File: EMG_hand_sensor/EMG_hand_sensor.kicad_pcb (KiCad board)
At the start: 2 copper layers, 39 parts, among them J1 Conn_2Rows-07Pins_Shielded, J2 B2B-XH-A, U1 TVS0500DRV, U10 TRS_AUDIO_JACK_3.5mm, U11 TRS_AUDIO_JACK_3.5mm, U2 ADA4099-2xR, U3 CD74HC4067M, U4 TRS_AUDIO_JACK_3.5mm, U6 ADA4099-2xR, U7 LT1762, U8 TRS_AUDIO_JACK_3.5mm

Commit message: new schematic done
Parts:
- removed R11, R16: 15k, Resistor_SMD:R_0805_2012Metric_Pad1.20x1.40mm_HandSolder
- removed R12, R14, R15, R17, R18: 10k, Resistor_SMD:R_0805_2012Metric_Pad1.20x1.40mm_HandSolder
- removed R13: 100R, Resistor_SMD:R_0805_2012Metric_Pad1.20x1.40mm_HandSolder
- added C12: 1uF, Capacitor_SMD:C_0805_2012Metric_Pad1.18x1.45mm_HandSolder, F.Cu at (172.6, 95.6)
- added C13: 100n, Capacitor_SMD:C_0805_2012Metric_Pad1.18x1.45mm_HandSolder, F.Cu at (172.6, 98.6)
- added C14: 10p, Capacitor_SMD:C_0805_2012Metric_Pad1.18x1.45mm_HandSolder, F.Cu at (172.6, 101.6)
- added C15: 10p, Capacitor_SMD:C_0805_2012Metric_Pad1.18x1.45mm_HandSolder, F.Cu at (172.6, 104.6)
- added C7: 10nF, Capacitor_SMD:C_0805_2012Metric_Pad1.18x1.45mm_HandSolder, F.Cu at (167.8, 98.6)
- added D1: RED, Diode_SMD:D_0805_2012Metric, F.Cu at (141.7, 113.7)
- added FB1: 120R, Resistor_SMD:R_0805_2012Metric_Pad1.20x1.40mm_HandSolder, F.Cu at (141.8, 88.1)
- added SW1: SW_SPDT, Relay_THT:Relay_SPDT_Omron_G6E, F.Cu at (151.0, 89.2)
- added U5: INA128, INA:SOIC127P600X175-8N, F.Cu at (135.2, 96.5)
- added U9: INA128, INA:SOIC127P600X175-8N, F.Cu at (135.2, 109.5)
- added Y1: 16MHz, Crystal:Crystal_SMD_3225-4Pin_3.2x2.5mm, F.Cu at (170.6, 111.4)
- C1: value 100nF -> 10uF
- C2: value 10uF -> 100nF
- C3: value 33nF -> 100nF
- C4, C5: value 470nF -> 100nF
- C6: value 1uF -> 100nF
- C8: value 33nF -> 1uF
- J1: value Conn_2Rows-07Pins_Shielded -> USB_C_Receptacle_USB2.0_16P; footprint Connector_PinHeader_2.54mm:PinHeader_1x07_P2.54mm_Vertical_SMD_Pin1Left -> Connector_Molex:Molex_CLIK-Mate_502386-0970_1x09-1MP_P1.25mm_Horizontal
- J2: value B2B-XH-A -> Conn_01x04_Pin; footprint Connector_JST:JST_EH_B2B-EH-A_1x02_P2.50mm_Vertical -> Connector_PinHeader_2.54mm:PinHeader_1x04_P2.54mm_Vertical
- R10, R5: value 10k -> 500
- R2: value 1k -> 1k5
- R6: value 1k -> 500
- R7: value 18k -> 500
- R8, R9: value 10k -> 5k1
- U1: value TVS0500DRV -> USBLC6-2SC6; footprint Package_SON:WSON-6-1EP_2x2mm_P0.65mm_EP1x1.6mm -> Package_TO_SOT_SMD:SOT-23-6
- U2: value ADA4099-2xR -> STM32F103C8Tx; footprint Package_SO:SOIC-8_3.9x4.9mm_P1.27mm -> Package_QFP:LQFP-48_7x7mm_P0.5mm
- U3: value CD74HC4067M -> INA128; footprint Package_SO:SOIC-24W_7.5x15.4mm_P1.27mm -> INA:SOIC127P600X175-8N
- U6: value ADA4099-2xR -> INA128; footprint Package_SO:SOIC-8_3.9x4.9mm_P1.27mm -> INA:SOIC127P600X175-8N
- moved C11 83.4 mm to (167.8, 107.6)
- moved C8 83.4 mm to (167.8, 101.6)
- moved C9 83.4 mm to (167.8, 104.6)
- moved C6 83.1 mm to (167.8, 95.6)
- moved C1 80.9 mm to (163.0, 95.6)
- moved C2 80.9 mm to (163.0, 98.6)
- moved C3 80.9 mm to (163.0, 101.6)
- moved C4 80.9 mm to (163.0, 104.6)
- moved C5 80.9 mm to (163.0, 107.6)
- moved J2 64.5 mm to (177.3, 96.4)
- moved J1 63.9 mm to (168.9, 90.3)
- moved U7 61.2 mm to (164.3, 111.5)
- moved R6 57.0 mm to (146.6, 88.1)
- moved R7 57.0 mm to (146.6, 91.0)
- moved R10 55.7 mm to (146.6, 99.9)
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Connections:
- C1 pad 1: +3V3 -> +3.3V
- C10 pad 1: /+3v3 -> +3.3V
- C11 pad 1: /+3v3 -> +3.3V
- C2 pad 1: +3V3 -> +3.3V
- C3 pad 1: Net-(C3-Pad1) -> +3.3V
- C3 pad 2: EMG_analog_signal -> GND
- C4 pad 1: Net-(C4-Pad1) -> +3.3V
- C4 pad 2: Net-(U2B-+) -> GND
- C5 pad 1: EMG_analog_signal -> +3.3V
- C5 pad 2: Net-(C4-Pad1) -> GND
- C6 pad 1: EMG_analog_signal -> +3.3V
- C8 pad 1: Net-(U6A-+) -> +3.3VA
- C9 pad 1: /VBAT -> VBUS
- J1 pad 1: ¬Enable -> (no net)
- J1 pad 2: EMG_analog_signal -> (no net)
- J1 pad 3: S0 -> (no net)
- J1 pad 4: S2 -> (no net)
- J1 pad 5: S1 -> (no net)
- J1 pad 6: GND -> (no net)
- J1 pad 7: S3 -> (no net)
- J2 pad 1: GND -> +3.3V
- J2 pad 2: /VBAT -> /SWDIO
- R1 pad 1: EMG_analog_signal -> /SW_BOOT0
- R1 pad 2: Net-(C3-Pad1) -> /BOOT0
- R10 pad 2: Net-(U2B--) -> Net-(R10-Pad2)
- R2 pad 1: EMG_analog_signal -> Net-(D1-K)
- R2 pad 2: Net-(U6A--) -> GND
- R3 pad 1: Net-(U6A--) -> +3.3V
- R3 pad 2: GND -> /+1v6
- R4 pad 1: S3 -> /+1v6
- R5 pad 1: S2 -> Net-(R5-Pad1)
- R5 pad 2: GND -> Net-(R5-Pad2)
- R6 pad 1: EMG_analog_signal -> Net-(R6-Pad1)
- R6 pad 2: Net-(R10-Pad1) -> Net-(R6-Pad2)
- R7 pad 1: Net-(U2B--) -> Net-(R7-Pad1)
- R7 pad 2: GND -> Net-(R7-Pad2)
- R8 pad 1: GND -> Net-(J1-CC1)
- R8 pad 2: S0 -> GND
- R9 pad 1: Net-(U6A-+) -> /CC2
- R9 pad 2: Net-(C3-Pad1) -> GND
- U1 pad 1: GND -> Net-(J1-D--PadA7)
- U1 pad 3: GND -> Net-(J1-D+-PadA6)
- U1 pad 4: EMG_analog_signal -> /USB_D+
- U1 pad 5: EMG_analog_signal -> VBUS
- U1 pad 6: EMG_analog_signal -> /USB_D-
- U2 pad 1: EMG_analog_signal -> +3.3V
- U2 pad 2: EMG_analog_signal -> unconnected-(U2-PC13-Pad2)
- U2 pad 3: EMG_analog_signal -> unconnected-(U2-PC14-Pad3)
- U2 pad 4: (no net) -> unconnected-(U2-PC15-Pad4)
- U2 pad 5: Net-(U2B-+) -> /HSE_IN
- U2 pad 6: Net-(U2B--) -> /HSE_LOW
- U2 pad 7: Net-(R10-Pad1) -> /NRST
- U2 pad 8: (no net) -> GND
- U3 pad 1: EMG_analog_signal -> Net-(R5-Pad1)
- U3 pad 2: E8 -> E2
- U3 pad 3: E7 -> E1
- U3 pad 4: E6 -> GND
- U3 pad 5: E5 -> /+1v6
- U3 pad 6: E4 -> E1
- U3 pad 7: E3 -> +3.3V
- U3 pad 8: E2 -> Net-(R5-Pad2)
- U6 pad 1: EMG_analog_signal -> Net-(R7-Pad1)
- U6 pad 2: Net-(U6A--) -> E4
- U6 pad 3: Net-(U6A-+) -> E3
- U6 pad 4: (no net) -> GND
- U6 pad 5: EMG_analog_signal -> /+1v6
- U6 pad 6: Net-(U6B--) -> E3
- U6 pad 7: EMG_analog_signal -> +3.3V
- U6 pad 8: (no net) -> Net-(R7-Pad2)
- U7 pad 1: /+3v3 -> +3.3V
- U7 pad 2: /+3v3 -> +3.3V
- U7 pad 5: /VBAT -> VBUS
- U7 pad 8: /VBAT -> VBUS

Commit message: pcb design started layout
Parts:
- moved U6 62.8 mm to (196.3, 88.4)
- moved U5 61.2 mm to (193.0, 76.5)
- moved U4 58.7 mm to (194.6, 65.3), turned to 90 degrees
- moved U9 52.0 mm to (186.3, 99.9)
- moved SW1 48.7 mm to (134.0, 43.5)
- moved U10 45.9 mm to (194.0, 109.5), turned to -90 degrees
- moved U3 45.1 mm to (178.3, 76.6)
- moved D1 43.6 mm to (168.1, 79.0)
- moved J2 37.1 mm to (148.9, 72.5), turned to 90 degrees
- moved U11 35.8 mm to (208.3, 86.6)
- moved U2 31.2 mm to (176.7, 87.8)
- moved U1 28.2 mm to (162.9, 86.5)
- moved U8 26.6 mm to (172.9, 64.8), turned to -90 degrees
- moved J1 26.1 mm to (143.2, 86.0), turned to -90 degrees
- moved R1 20.7 mm to (124.2, 80.1)
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
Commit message: starting pch layout
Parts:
- removed U10, U11, U4, U8: TRS_AUDIO_JACK_3.5mm, Connector_Audio:Jack_3.5mm_CUI_SJ-3523-SMT_Horizontal
- added J3: AudioJack3, Connector_Audio:Jack_3.5mm_CUI_SJ-3523-SMT_Horizontal, F.Cu at (203.0, 102.0)
- added J4: AudioJack3, Connector_Audio:Jack_3.5mm_CUI_SJ-3523-SMT_Horizontal, F.Cu at (183.0, 64.0)
- added J5: AudioJack3, Connector_Audio:Jack_3.5mm_CUI_SJ-3523-SMT_Horizontal, F.Cu at (162.4, 66.3)
- added J6: AudioJack3, Connector_Audio:Jack_3.5mm_CUI_SJ-3523-SMT_Horizontal, F.Cu at (203.0, 78.5)
- J1: footprint Connector_Molex:Molex_CLIK-Mate_502386-0970_1x09-1MP_P1.25mm_Horizontal -> Connector_USB:USB_C_Receptacle_GCT_USB4105-xx-A_16P_TopMnt_Horizontal
- SW1: footprint Relay_THT:Relay_SPDT_Omron_G6E -> Button_Switch_SMD:SW_SPDT_CK_JS102011SAQN
- moved C15 91.9 mm to (74.3, 99.5)
- moved SW1 71.6 mm to (177.0, 100.8)
- moved D1 49.9 mm to (120.4, 64.0)
- moved J2 30.5 mm to (169.5, 95.0), turned to 0 degrees
- moved C11 24.7 mm to (142.5, 132.0)
- moved C13 24.7 mm to (147.3, 123.0)
- moved C14 24.7 mm to (147.3, 126.0)
- moved C2 24.7 mm to (137.7, 123.0)
- moved C3 24.7 mm to (137.7, 126.0)
- moved C4 24.7 mm to (137.7, 129.0)
- moved C5 24.7 mm to (137.7, 132.0)
- moved C7 24.7 mm to (142.5, 123.0)
- moved C8 24.7 mm to (142.5, 126.0)
- moved C9 24.7 mm to (142.5, 129.0)
- moved C1 24.7 mm to (137.7, 120.0)
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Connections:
- U2 pad 10: E1 -> /O1
- U2 pad 11: E4 -> /O2
- U2 pad 12: E3 -> /O3
- U2 pad 13: E1 -> /O4
- U3 pad 2: E2 -> /E2
- U3 pad 3: E1 -> /E1
- U3 pad 6: E1 -> /O4
- U5 pad 2: E6 -> /E8
- U5 pad 3: E5 -> /E7
- U5 pad 6: E4 -> /O3
- U6 pad 2: E4 -> /E4
- U6 pad 3: E3 -> /E3
- U6 pad 6: E3 -> /O1
- U9 pad 2: E6 -> /E6
- U9 pad 3: E5 -> /E5
- U9 pad 6: E4 -> /O2

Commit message: design rules
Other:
- copper layers 2 -> 4
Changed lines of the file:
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@@
 	(generator_version "9.0")
 	(general
-		(thickness 1.6)
+		(thickness 1.6062)
 		(legacy_teardrops no)
 	)
@@
 	(layers
 		(0 "F.Cu" signal)
+		(4 "In1.Cu" signal)
+		(6 "In2.Cu" signal)
 		(2 "B.Cu" signal)
 		(9 "F.Adhes" user "F.Adhesive")
@@
 	)
 	(setup
+		(stackup
+			(layer "F.SilkS"
+				(type "Top Silk Screen")
+			)
+			(layer "F.Paste"
+				(type "Top Solder Paste")
+			)
+			(layer "F.Mask"
+				(type "Top Solder Mask")
+				(thickness 0.01)
+			)
+			(layer "F.Cu"
+				(type "copper")
+				(thickness 0.035)
+			)
+			(layer "dielectric 1"
+				(type "prepreg")
+				(thickness 0.2104)
+				(material "FR-4")
+				(epsilon_r 4.4)
+				(loss_tangent 0.02)
+			)
+			(layer "In1.Cu"
+				(type "copper")
+				(thickness 0.0152)
+			)
+			(layer "dielectric 2"
+				(type "core")
+				(thickness 1.065)
+				(material "FR-4")
+				(epsilon_r 4.6)
+				(loss_tangent 0.02)
+			)
+			(layer "In2.Cu"
+				(type "copper")
+				(thickness 0.0152)
+			)
+			(layer "dielectric 3"
+				(type "prepreg")
+				(thickness 0.2104)
+				(material "FR-4")
+				(epsilon_r 4.4)
+				(loss_tangent 0.02)
+			)
+			(layer "B.Cu"
+				(type "copper")
+				(thickness 0.035)
+			)
+			(layer "B.Mask"
+				(type "Bottom Solder Mask")
+				(thickness 0.01)
+			)
+			(layer "B.Paste"
+				(type "Bottom Solder Paste")
+			)
+			(layer "B.SilkS"
+				(type "Bottom Silk Screen")
+			)
+			(copper_finish "None")
+			(dielectric_constraints yes)
+		)
 		(pad_to_mask_clearance 0)
 		(allow_soldermask_bridges_in_footprints no)

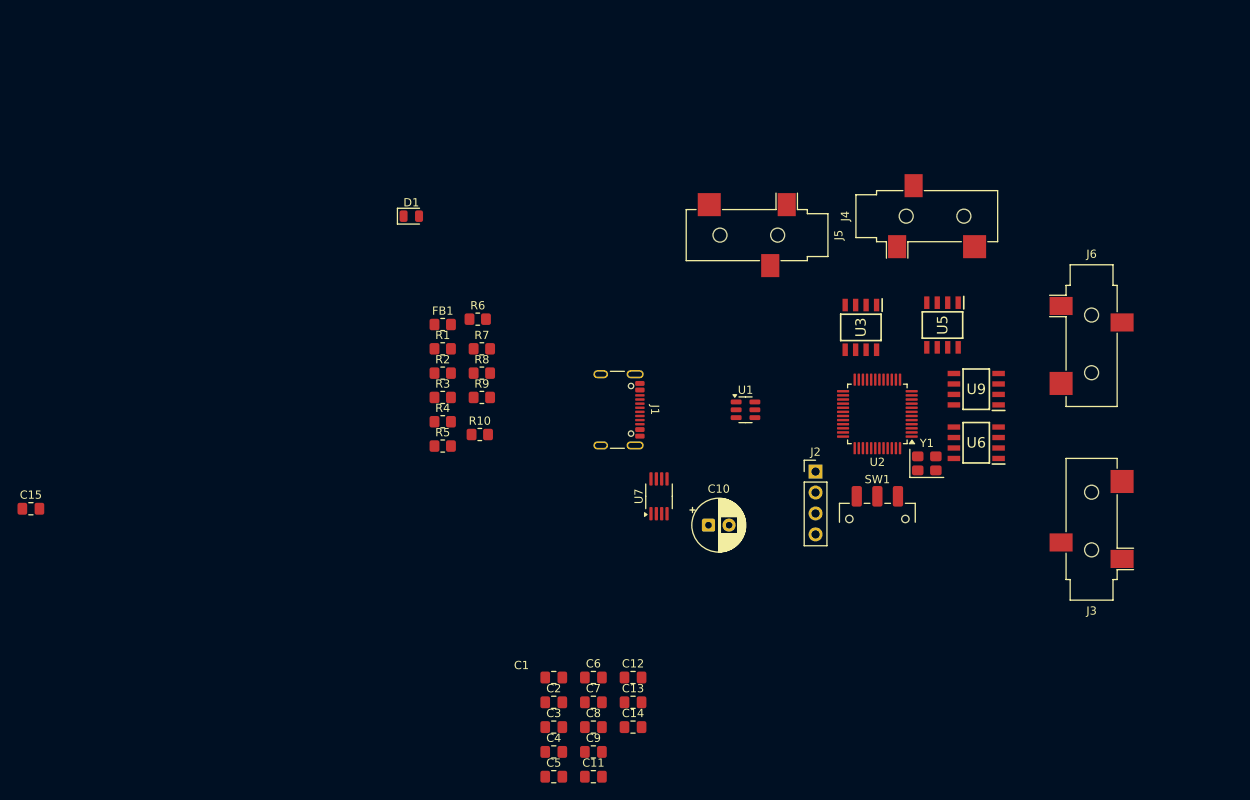
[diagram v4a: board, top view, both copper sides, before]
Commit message: pcb layout finished
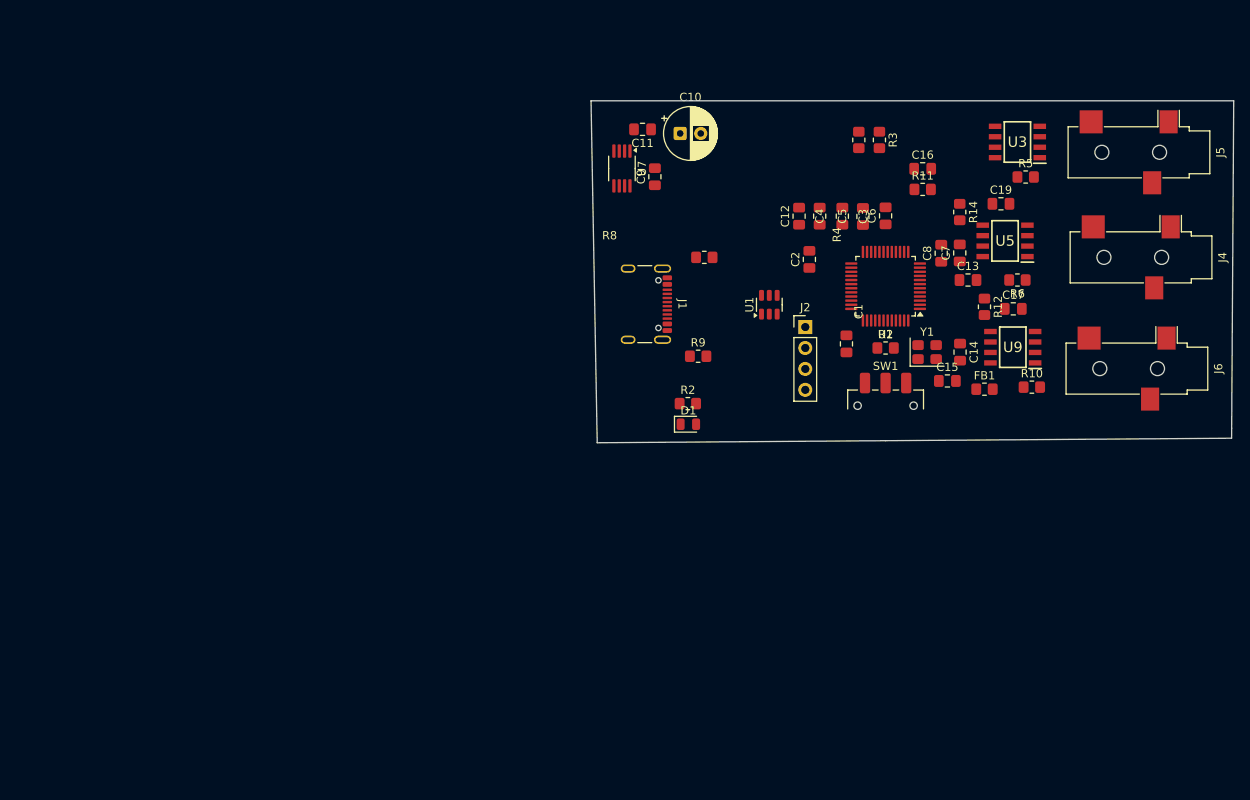
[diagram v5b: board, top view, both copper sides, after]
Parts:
- removed J3: AudioJack3, Connector_Audio:Jack_3.5mm_CUI_SJ-3523-SMT_Horizontal
- removed R7: 500, Resistor_SMD:R_0805_2012Metric_Pad1.20x1.40mm_HandSolder
- removed U6: INA128, INA:SOIC127P600X175-8N
- added C16: 100nF, Capacitor_SMD:C_0805_2012Metric_Pad1.18x1.45mm_HandSolder, F.Cu at (182.5, 58.2)
- added C17: 100nF, Capacitor_SMD:C_0805_2012Metric_Pad1.18x1.45mm_HandSolder, F.Cu at (193.5, 75.2)
- added C19: 100nF, Capacitor_SMD:C_0805_2012Metric_Pad1.18x1.45mm_HandSolder, F.Cu at (192.0, 62.5)
- added R11: 3.3k, Resistor_SMD:R_0805_2012Metric_Pad1.20x1.40mm_HandSolder, F.Cu at (182.5, 60.8)
- added R12: 3.3k, Resistor_SMD:R_0805_2012Metric_Pad1.20x1.40mm_HandSolder, F.Cu at (190.0, 75.0)
- added R14: 3.3k, Resistor_SMD:R_0805_2012Metric_Pad1.20x1.40mm_HandSolder, F.Cu at (187.0, 63.5)
- R10, R5, R6: value 500 -> 50R
- moved C15 112.3 mm to (185.5, 84.0)
- moved C11 78.8 mm to (148.5, 53.5), turned to 180 degrees
- moved R5 77.9 mm to (195.0, 59.2)
- moved C5 76.5 mm to (172.8, 64.0), turned to 90 degrees
- moved C4 72.6 mm to (170.0, 64.0), turned to 90 degrees
- moved C3 72.4 mm to (175.2, 64.0), turned to 90 degrees
- moved C8 71.3 mm to (184.8, 68.5), turned to 90 degrees
- moved C7 70.4 mm to (187.0, 68.5), turned to 90 degrees
- moved C9 70.2 mm to (150.0, 59.2), turned to 90 degrees
- moved R10 67.2 mm to (195.8, 84.8)
- moved C6 66.3 mm to (178.0, 64.0), turned to 90 degrees
- moved FB1 66.2 mm to (190.0, 85.0)
- moved R6 65.7 mm to (194.0, 71.8), turned to 180 degrees
- moved C13 65.4 mm to (188.0, 71.8)
- moved C2 62.1 mm to (168.8, 69.2), turned to 90 degrees
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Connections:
- net /+1v6 renamed +1V6
- net /SWCLK renamed /SWD_CLK
- net /SWDIO renamed /SWD_IO
- J1 pad A6: Net-(J1-D+-PadA6) -> /USB_D+
- J1 pad A7: Net-(J1-D--PadA7) -> /USB_D-
- J1 pad B6: Net-(J1-D+-PadA6) -> /USB_D+
- J1 pad B7: Net-(J1-D--PadA7) -> /USB_D-
- U1 pad 1: Net-(J1-D--PadA7) -> /USB_D-
- U1 pad 3: Net-(J1-D+-PadA6) -> /USB_D+
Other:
- board outline added: 78 x 41.5 mm

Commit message: routing time
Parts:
- moved R5 6.40 mm to (191.0, 54.2), turned to -90 degrees
- moved R10 5.70 mm to (191.2, 81.2), turned to -90 degrees
- moved C10 5.26 mm to (156.6, 57.9)
- moved C11 5.26 mm to (152.0, 57.4)
- moved C9 5.26 mm to (153.5, 63.1)
- moved U7 5.26 mm to (149.5, 62.1)
- moved R3 4.25 mm to (173.5, 56.8)
- moved R4 4.25 mm to (171.0, 56.8)
- moved FB1 3.95 mm to (187.8, 88.2)
- moved U9 2.61 mm to (195.5, 81.5), turned to -90 degrees
- moved U3 1.77 mm to (195.8, 54.8), turned to -90 degrees
- moved C19 1.00 mm to (191.0, 62.5)
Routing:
- net /E6: track 0.00 -> 1.49 mm
- added copper zone on In1.Cu, net GND
- added copper zone on In2.Cu, net GND

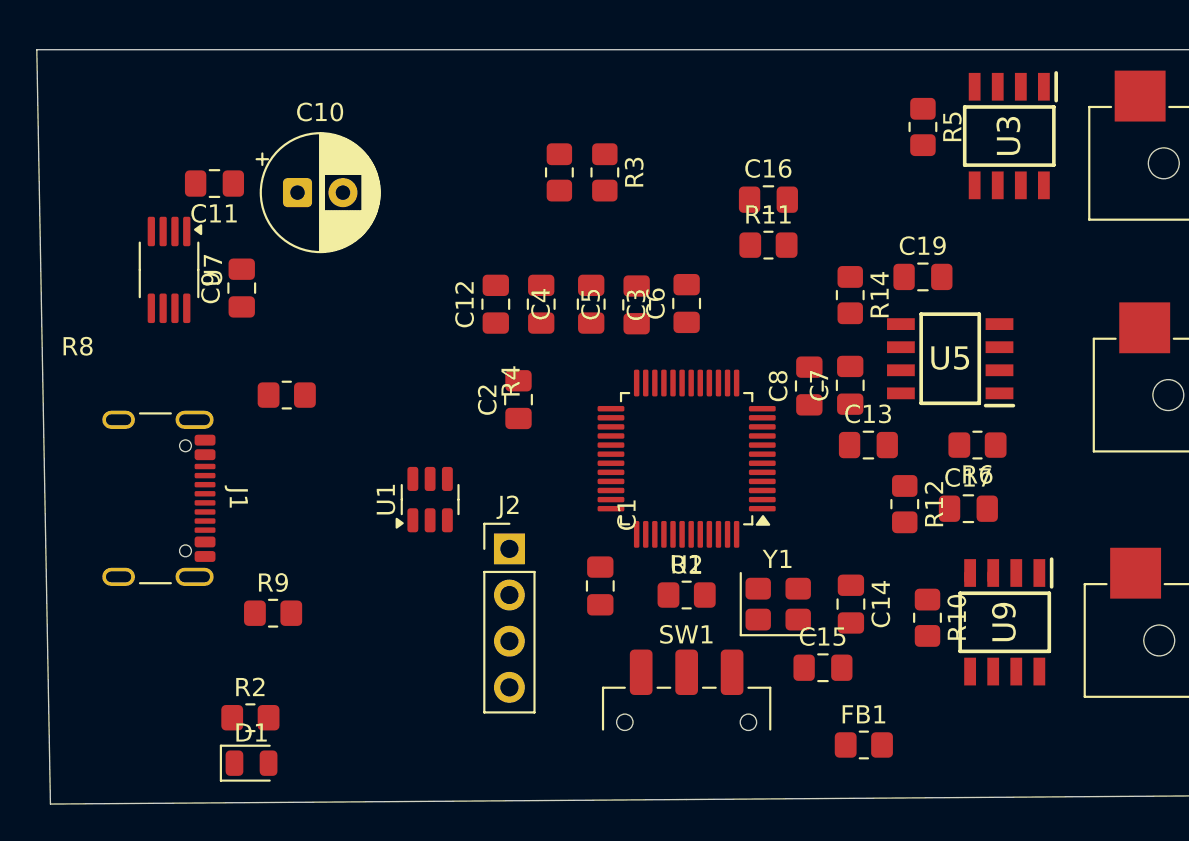
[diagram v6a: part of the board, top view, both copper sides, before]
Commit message: Need to add guard traces and vias and then I can start routing
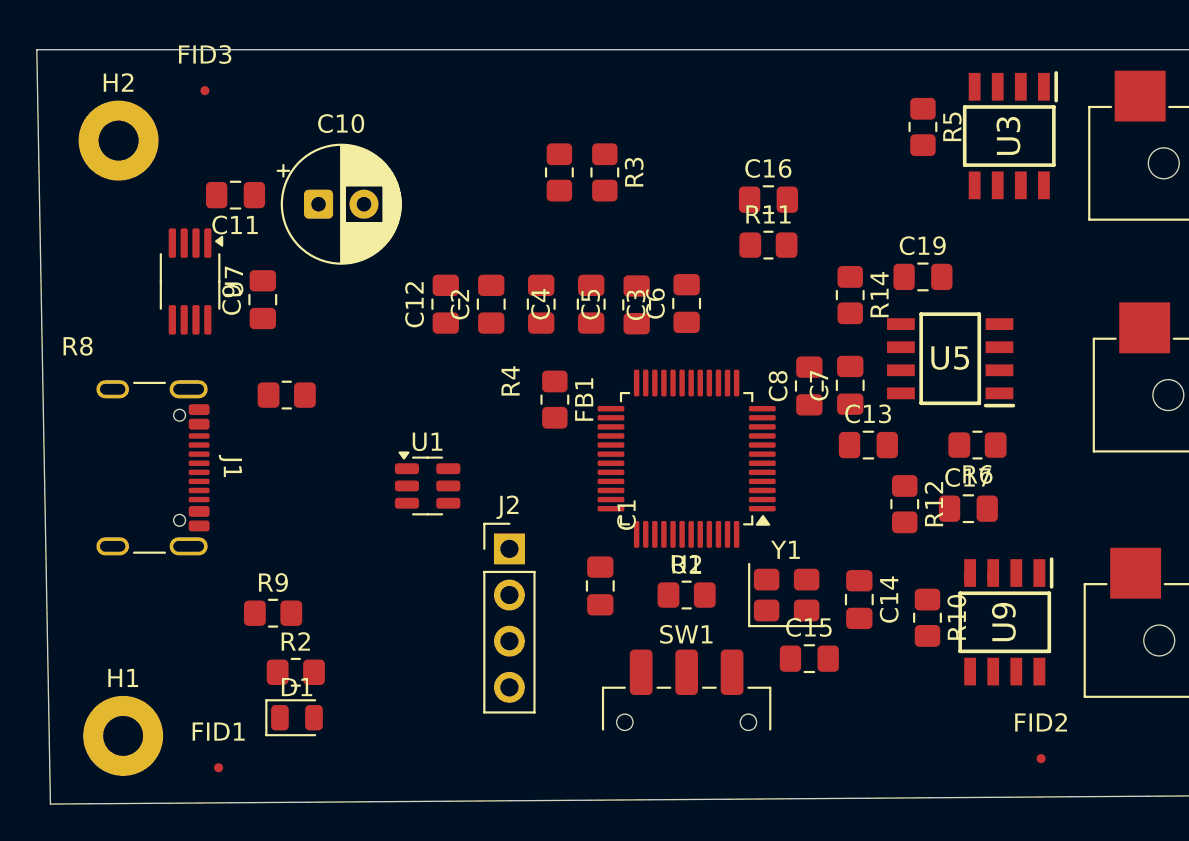
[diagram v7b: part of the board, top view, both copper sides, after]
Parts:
- added FID1: Fiducial, Fiducial:Fiducial_0.5mm_Mask2mm, F.Cu at (152.2, 89.5)
- added FID2: Fiducial, Fiducial:Fiducial_0.5mm_Mask2mm, F.Cu at (197.5, 89.0)
- added FID3: Fiducial, Fiducial:Fiducial_0.5mm_Mask2mm, F.Cu at (151.5, 52.2)
- added H1: MountingHole_Pad, MountingHole:MountingHole_2.2mm_M2_Pad, F.Cu at (147.0, 87.8)
- added H2: MountingHole_Pad, MountingHole:MountingHole_2.2mm_M2_Pad, F.Cu at (146.8, 55.0)
- moved FB1 25.5 mm to (170.8, 69.2), turned to -90 degrees
- moved C2 5.46 mm to (167.2, 64.0)
- moved D1 3.54 mm to (156.6, 86.8)
- moved R2 3.54 mm to (156.5, 84.2)
- moved C12 2.75 mm to (164.8, 64.0)
- moved J1 1.71 mm to (147.5, 73.0)
- moved C10 1.32 mm to (157.8, 58.5)
- moved C11 1.32 mm to (153.2, 58.0)
- moved C9 1.32 mm to (154.7, 63.8)
- moved U7 1.32 mm to (150.7, 62.8)
- moved C15 0.90 mm to (184.8, 83.5)
- moved U1 0.76 mm to (163.8, 74.0), turned to 0 degrees
- moved Y1 0.68 mm to (183.5, 80.0)
- moved C14 0.53 mm to (187.5, 80.2)
